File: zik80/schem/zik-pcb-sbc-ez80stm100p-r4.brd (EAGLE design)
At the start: 149.8 x 98.7 mm, 107 parts, among them IC1 7432N, IC2 7404N

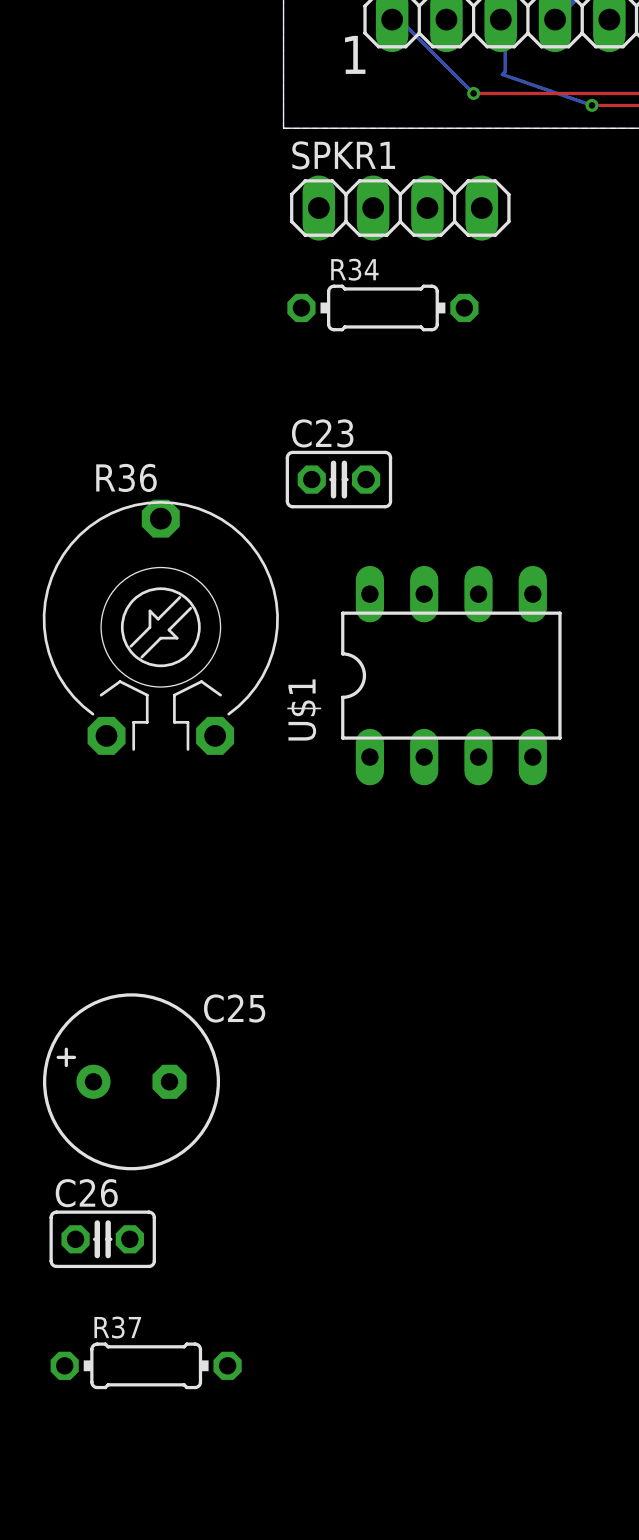
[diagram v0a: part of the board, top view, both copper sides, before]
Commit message: adding a audio circuit schem image
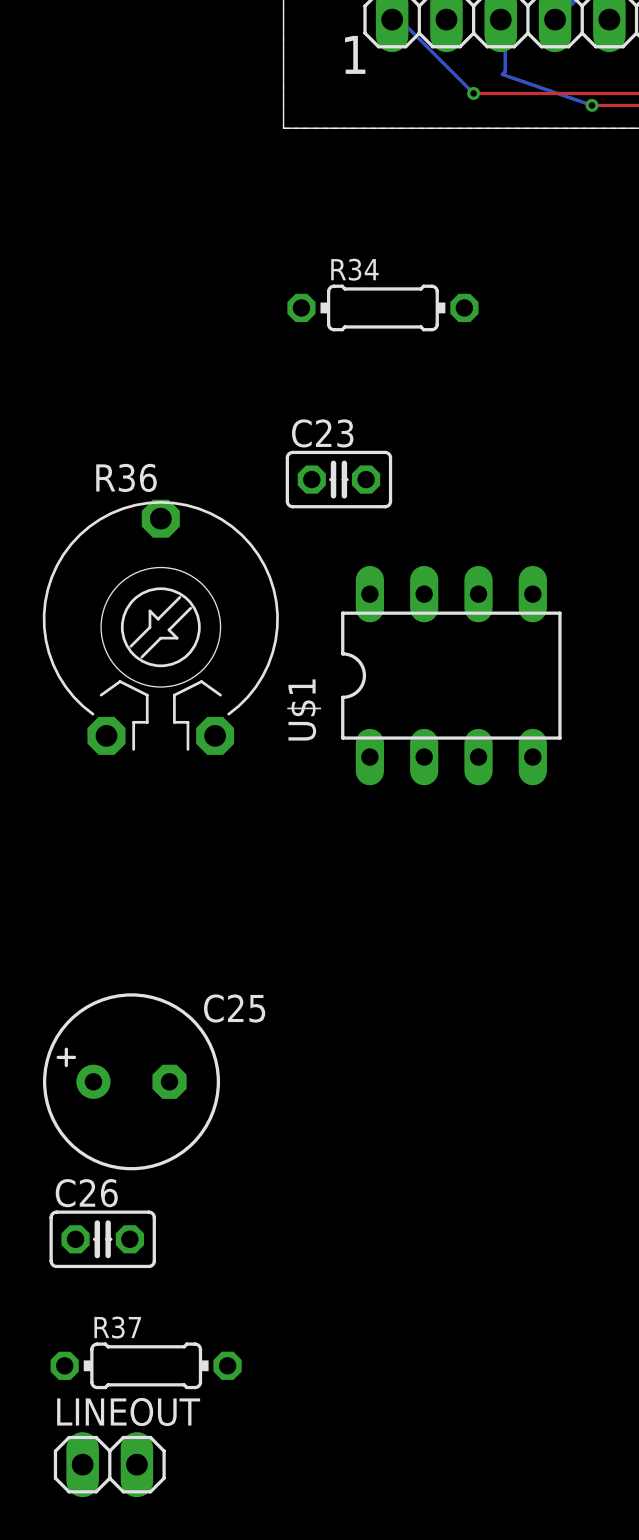
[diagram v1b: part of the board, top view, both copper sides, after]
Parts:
- removed SPKR1: (no value), pinhead:1X04
- added LINEOUT: (no value), pinhead:1X02
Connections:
- new net N$3: LINEOUT.2, U$1.7
- net GND: now also LINEOUT.1
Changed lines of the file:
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@@
 </element>
 <element name="3V" library="wirepad" package="SMD1,27-2,54" value="WIREPADSMD1,27-254" x="55.6006" y="56.388"/>
-<element name="SPKR1" library="pinhead" package="1X04" value="" x="5.461" y="-3.7338"/>
 <element name="R34" library="rcl" package="0204/7" value="1K" x="4.6482" y="-8.4074"/>
 <element name="C23" library="rcl" package="C025-025X050" value="100uF" x="2.5908" y="-16.4338"/>
@@
 <element name="C26" library="rcl" package="C025-025X050" value=".05uF" x="-8.4582" y="-51.9684"/>
 <element name="R37" library="rcl" package="0204/7" value="10" x="-6.4262" y="-57.8866"/>
+<element name="LINEOUT" library="pinhead" package="1X02" value="" x="-8.128" y="-62.5094"/>
 </elements>
 <signals>
@@
 <contactref element="U$1" pad="4"/>
 <contactref element="R37" pad="1"/>
+<contactref element="LINEOUT" pad="1"/>
 <wire x1="132.08" y1="92.71" x2="133.096" y2="92.964" width="0" layer="19" extent="16-16"/>
 <wire x1="137.922" y1="77.343" x2="136.49325" y2="87.97925" width="0" layer="19" extent="1-1"/>
@@
 <wire x1="-3.2004" y1="-28.4226" x2="6.5786" y2="-29.4132" width="0" layer="19" extent="1-1"/>
 <wire x1="-10.2362" y1="-57.8866" x2="-3.2004" y2="-28.4226" width="0" layer="19" extent="1-1"/>
+<wire x1="-9.398" y1="-62.5094" x2="-10.2362" y2="-57.8866" width="0" layer="19" extent="1-1"/>
 </signal>
 <signal name="+3V3">
@@
 <wire x1="-2.6162" y1="-57.8866" x2="-9.7282" y2="-51.9684" width="0" layer="19" extent="1-1"/>
 </signal>
+<signal name="N$3">
+<contactref element="U$1" pad="7"/>
+<contactref element="LINEOUT" pad="2"/>
+<wire x1="6.5786" y1="-21.7932" x2="-6.858" y2="-62.5094" width="0" layer="19" extent="1-1"/>
+</signal>
 </signals>
